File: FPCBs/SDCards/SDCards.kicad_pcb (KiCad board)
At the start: 2 copper layers, 14.7 x 20.5 mm, 4 parts, among them J1 SD_Card_Device, J2 SD_Card_Device, J3 SD_Card_Device, J4 SD_Card_Device

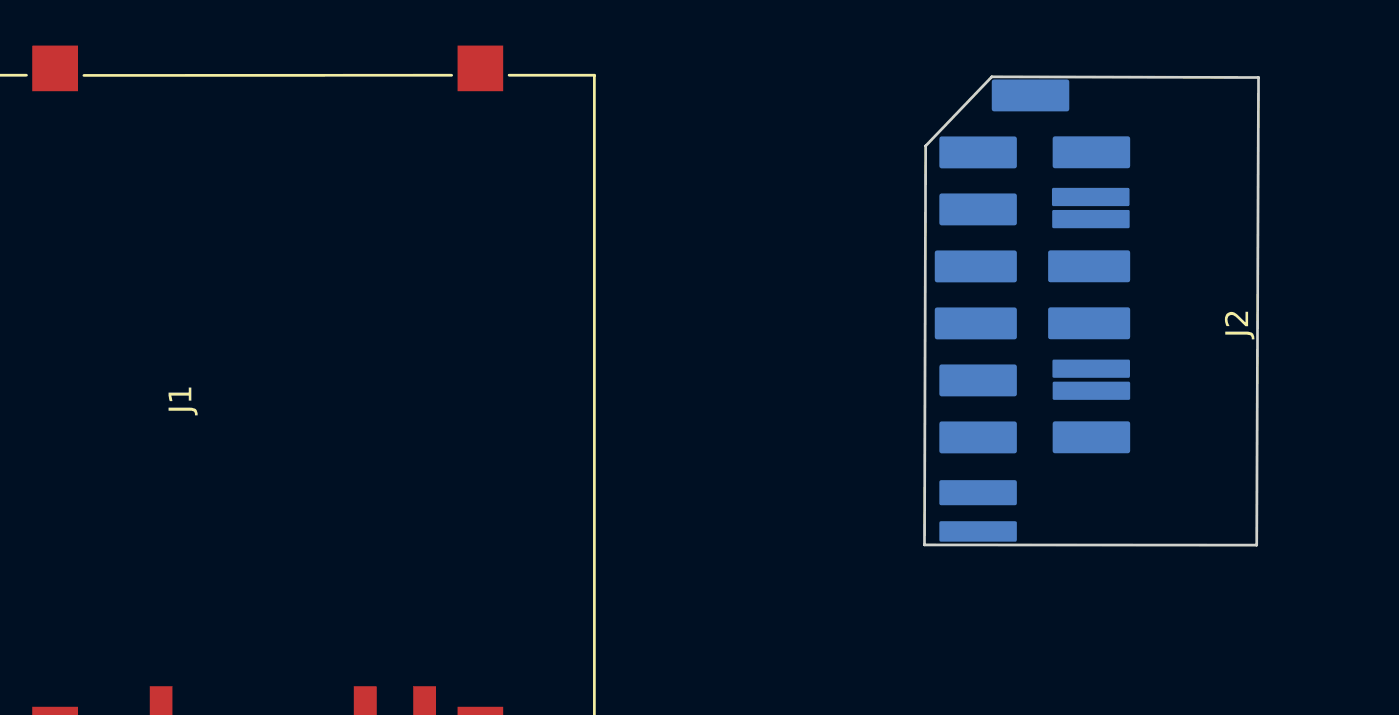
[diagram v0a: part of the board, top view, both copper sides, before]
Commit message: Add pad mask
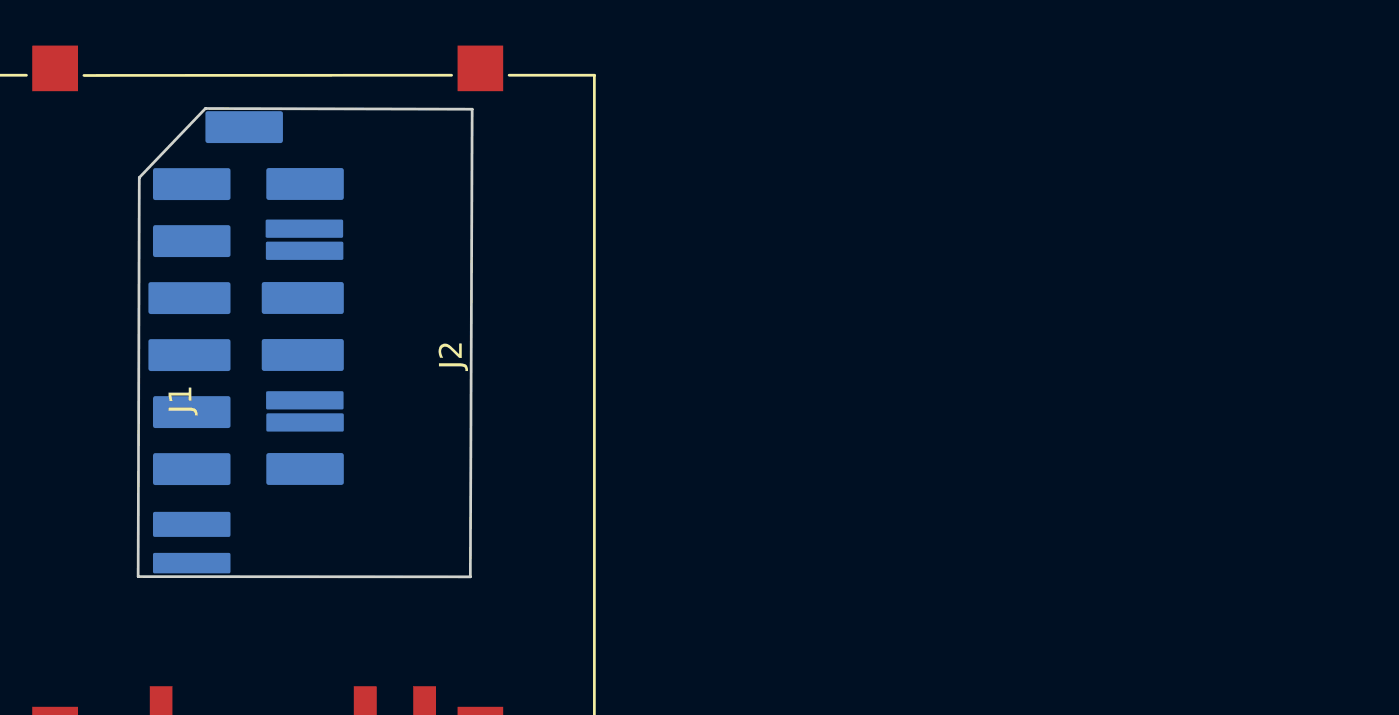
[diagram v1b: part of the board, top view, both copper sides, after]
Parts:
- moved J2 34.5 mm to (82.6, 77.7)
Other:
- outline, holes or cut-outs redrawn
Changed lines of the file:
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@@
 	(footprint "Leica-G9ii:SD_Card_Chip_UHS-II"
 		(layer "F.Cu")
-		(at 117.09 76.325 90)
+		(at 82.6 77.715 90)
 		(descr "SD card device PCB layout, contacts and mechanicalm, 16mm slot depth. Manufacture with PCB thickness of 1.4mm, http://www.convict.lu/pdf/ProdManualSDCardv1.9.pdf")
 		(tags "SD Card")

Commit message: sd card
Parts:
- moved J4 49.9 mm to (89.0, 147.7)
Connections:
- J1 pad 11: (no net) -> Net-(J1-D0+)
- J1 pad 12: (no net) -> Net-(J1-D0-)
- J1 pad 13: (no net) -> Net-(J1-VSS4)
- J1 pad 14: (no net) -> Net-(J1-VDD2)
- J1 pad 15: (no net) -> Net-(J1-D1-)
- J1 pad 16: (no net) -> Net-(J1-D1+)
- J1 pad 17: (no net) -> Net-(J1-Name)
- J1 pad 3: Net-(J1-VSS-Pad3) -> Net-(J1-VSS1)
- J1 pad 6: Net-(J1-VSS-Pad3) -> Net-(J1-VSS2)
- J2 pad 10: (no net) -> Net-(J1-VSS3)
- J2 pad 11: (no net) -> Net-(J1-D0+)
- J2 pad 12: (no net) -> Net-(J1-D0-)
- J2 pad 13: (no net) -> Net-(J1-VSS4)
- J2 pad 14: (no net) -> Net-(J1-VDD2)
- J2 pad 15: (no net) -> Net-(J1-D1-)
- J2 pad 16: (no net) -> Net-(J1-D1+)
- J2 pad 17: (no net) -> Net-(J1-Name)
- J2 pad 3: Net-(J1-VSS-Pad3) -> Net-(J1-VSS1)
- J2 pad 6: Net-(J1-VSS-Pad3) -> Net-(J1-VSS2)
- J3 pad 11: (no net) -> Net-(J3-D0+)
- J3 pad 12: (no net) -> Net-(J3-D0-)
- J3 pad 13: (no net) -> Net-(J3-VSS4)
- J3 pad 14: (no net) -> Net-(J3-VDD2)
- J3 pad 15: (no net) -> Net-(J3-D1-)
- J3 pad 16: (no net) -> Net-(J3-D1+)
- J3 pad 17: (no net) -> Net-(J3-Name)
- J3 pad 3: Net-(J3-VSS-Pad3) -> Net-(J3-VSS1)
- J3 pad 6: Net-(J3-VSS-Pad3) -> Net-(J3-VSS2)
- J4 pad 11: (no net) -> Net-(J3-D0+)
- J4 pad 12: (no net) -> Net-(J3-D0-)
- J4 pad 13: (no net) -> Net-(J3-VSS4)
- J4 pad 14: (no net) -> Net-(J3-VDD2)
- J4 pad 15: (no net) -> Net-(J3-D1-)
- J4 pad 16: (no net) -> Net-(J3-D1+)
- J4 pad 17: (no net) -> Net-(J3-Name)
- J4 pad 3: Net-(J3-VSS-Pad3) -> Net-(J3-VSS1)
- J4 pad 6: Net-(J3-VSS-Pad3) -> Net-(J3-VSS2)
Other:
- board size 14.7 x 20.5 mm -> 45 x 77.4 mm
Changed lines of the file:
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@@
 	(net 2 "Net-(J1-CD{slash}DAT3)")
 	(net 3 "Net-(J1-DAT0)")
-	(net 4 "Net-(J1-VSS-Pad3)")
+	(net 4 "Net-(J1-VDD2)")
 	(net 5 "Net-(J1-CMD)")
 	(net 6 "Net-(J1-DAT1)")
@@
 	(net 8 "Net-(J1-CLK)")
 	(net 9 "Net-(J3-DAT2)")
-	(net 10 "Net-(J3-VSS-Pad3)")
+	(net 10 "Net-(J1-D0-)")
 	(net 11 "Net-(J3-DAT1)")
 	(net 12 "Net-(J3-CLK)")
@@
 	(net 15 "Net-(J3-DAT0)")
 	(net 16 "Net-(J3-CMD)")
+	(net 17 "Net-(J1-VSS4)")
+	(net 18 "Net-(J1-Name)")
+	(net 19 "Net-(J1-VSS1)")
+	(net 20 "Net-(J1-VSS2)")
+	(net 21 "Net-(J1-D0+)")
+	(net 22 "Net-(J1-D1+)")
+	(net 23 "Net-(J1-D1-)")
+	(net 24 "Net-(J1-VSS3)")
+	(net 25 "Net-(J3-VSS2)")
+	(net 26 "Net-(J3-VSS4)")
+	(net 27 "Net-(J3-Name)")
+	(net 28 "Net-(J3-VSS1)")
+	(net 29 "Net-(J3-D0+)")
+	(net 30 "Net-(J3-D1-)")
+	(net 31 "Net-(J3-D0-)")
+	(net 32 "Net-(J3-VDD2)")
+	(net 33 "Net-(J3-D1+)")
 	(footprint "Leica-G9ii:SD_Card_Socket_UHS-II_HTK_AXA573062"
 		(layer "F.Cu")
-		(at 126.44 114.65)
+		(at 89.03 147.69)
 		(descr "SD, SMD, top-mount, push-push (https://www.hirose.com/product/document?clcode=CL0609-0004-8-82&productname=DM1AA-SF-PEJ(82)&series=DM1&documenttype=2DDrawing&lang=en&documentid=0000915301)")
 		(tags "SD card connector")
@@
 			)
 		)
-		(property "Description" "SD card device/card"
+		(property "Description" "SD card UHS-II"
 			(at 0 0 0)
 			(unlocked yes)
@@
 			)
 		)
-		(property ki_fp_filters "SD*Device*")
+		(property ki_fp_filters "SD*")
 		(sheetname "/")
 		(sheetfile "SDCards.kicad_sch")
@@
 			(size 1 2)
 			(layers "F.Cu" "F.Mask" "F.Paste")
-			(net 10 "Net-(J3-VSS-Pad3)")
-			(pinfunction "VSS")
+			(net 28 "Net-(J3-VSS1)")
+			(pinfunction "VSS1")
 			(pintype "power_in")
 		)
@@
 			(size 1 2)
 			(layers "F.Cu" "F.Mask" "F.Paste")
-			(net 10 "Net-(J3-VSS-Pad3)")
-			(pinfunction "VSS")
-			(pintype "passive")
+			(net 25 "Net-(J3-VSS2)")
+			(pinfunction "VSS2")
+			(pintype "power_in")
 		)
 		(pad "7" smd rect
@@
 			(size 1 2)
 			(layers "F.Cu" "F.Mask" "F.Paste")
+			(net 29 "Net-(J3-D0+)")
+			(pinfunction "D0+")
+			(pintype "bidirectional")
 		)
 		(pad "12" smd rect
@@
 			(size 1 2)
 			(layers "F.Cu" "F.Mask" "F.Paste")
+			(net 31 "Net-(J3-D0-)")
+			(pinfunction "D0-")
+			(pintype "bidirectional")
 		)
 		(pad "13" smd rect
@@
 			(size 1 2)
 			(layers "F.Cu" "F.Mask" "F.Paste")
+			(net 26 "Net-(J3-VSS4)")
+			(pinfunction "VSS4")
+			(pintype "power_in")
 		)
 		(pad "14" smd rect
@@
 			(size 1 2)
 			(layers "F.Cu" "F.Mask" "F.Paste")
+			(net 32 "Net-(J3-VDD2)")
+			(pinfunction "VDD2")
+			(pintype "power_in")
 		)
 		(pad "15" smd rect
@@
 			(size 1 2)
 			(layers "F.Cu" "F.Mask" "F.Paste")
+			(net 30 "Net-(J3-D1-)")
+			(pinfunction "D1-")
+			(pintype "bidirectional")
 		)
 		(pad "16" smd rect
@@
 			(size 1 2)
 			(layers "F.Cu" "F.Mask" "F.Paste")
+			(net 33 "Net-(J3-D1+)")
+			(pinfunction "D1+")
+			(pintype "bidirectional")
 		)
 		(pad "17" smd rect
@@
 			(size 1 2)
 			(layers "F.Cu" "F.Mask" "F.Paste")
+			(net 27 "Net-(J3-Name)")
+			(pinfunction "Name")
+			(pintype "power_in")
 		)
 		(pad "CP" smd rect
@@
 			)
 		)
-		(property "Description" "SD card device/card"
+		(property "Description" "SD card UHS-II"
 			(at 0 0 90)
 			(unlocked yes)
@@
 			)
 		)
-		(property ki_fp_filters "SD*Device*")
+		(property ki_fp_filters "SD*")
 		(sheetname "/")
 		(sheetfile "SDCards.kicad_sch")
@@
 			(size 1 2)
 			(layers "F.Cu" "F.Mask" "F.Paste")
-			(net 10 "Net-(J3-VSS-Pad3)")
-			(pinfunction "VSS")
+			(net 28 "Net-(J3-VSS1)")
+			(pinfunction "VSS1")
 			(pintype "power_in")
 		)
@@
 			(size 1 2)
 			(layers "F.Cu" "F.Mask" "F.Paste")
-			(net 10 "Net-(J3-VSS-Pad3)")
-			(pinfunction "VSS")
-			(pintype "passive")
+			(net 25 "Net-(J3-VSS2)")
+			(pinfunction "VSS2")
+			(pintype "power_in")
 		)
 		(pad "7" smd rect
@@
 			(size 1 2)
 			(layers "F.Cu" "F.Mask" "F.Paste")
+			(net 29 "Net-(J3-D0+)")
+			(pinfunction "D0+")
+			(pintype "bidirectional")
 		)
 		(pad "12" smd rect
@@
 			(size 1 2)
 			(layers "F.Cu" "F.Mask" "F.Paste")
+			(net 31 "Net-(J3-D0-)")
+			(pinfunction "D0-")
+			(pintype "bidirectional")
 		)
 		(pad "13" smd rect
@@
 			(size 1 2)
 			(layers "F.Cu" "F.Mask" "F.Paste")
+			(net 26 "Net-(J3-VSS4)")
+			(pinfunction "VSS4")
+			(pintype "power_in")
 		)
 		(pad "14" smd rect
@@
 			(size 1 2)
 			(layers "F.Cu" "F.Mask" "F.Paste")
+			(net 32 "Net-(J3-VDD2)")
+			(pinfunction "VDD2")
+			(pintype "power_in")
 		)
 		(pad "15" smd rect
@@
 			(size 1 2)
 			(layers "F.Cu" "F.Mask" "F.Paste")
+			(net 30 "Net-(J3-D1-)")
+			(pinfunction "D1-")
+			(pintype "bidirectional")
 		)
 		(pad "16" smd rect
@@
 			(size 1 2)
 			(layers "F.Cu" "F.Mask" "F.Paste")
+			(net 33 "Net-(J3-D1+)")
+			(pinfunction "D1+")
+			(pintype "bidirectional")
 		)
 		(pad "17" smd rect
@@
 			(size 1 2)
 			(layers "F.Cu" "F.Mask" "F.Paste")
+			(net 27 "Net-(J3-Name)")
+			(pinfunction "Name")
+			(pintype "power_in")
 		)
 		(pad "CP" smd rect
@@
 			)
 		)
-		(property "Description" "SD card device/card"
+		(property "Description" "SD card UHS-II"
 			(at 0 17.55 90)
 			(unlocked yes)
@@
 			)
 		)
-		(property ki_fp_filters "SD*Device*")
+		(property ki_fp_filters "SD*")
 		(sheetname "/")
 		(sheetfile "SDCards.kicad_sch")
@@
 			(layers "B.Cu" "B.Mask")
 			(roundrect_rratio 0.07142857143)
-			(net 4 "Net-(J1-VSS-Pad3)")
-			(pinfunction "VSS")
+			(net 19 "Net-(J1-VSS1)")
+			(pinfunction "VSS1")
 			(pintype "power_in")
 			(clearance 0.05)
@@
 			(layers "B.Cu" "B.Mask")
 			(roundrect_rratio 0.07142857143)
-			(net 4 "Net-(J1-VSS-Pad3)")
-			(pinfunction "VSS")
-			(pintype "passive")
+			(net 20 "Net-(J1-VSS2)")
+			(pinfunction "VSS2")
+			(pintype "power_in")
 			(clearance 0.05)
 		)
@@
 			(layers "B.Cu" "B.Mask")
 			(roundrect_rratio 0.07142857143)
+			(net 24 "Net-(J1-VSS3)")
+			(pinfunction "VSS3")
+			(pintype "power_in")
 			(clearance 0.05)
 		)
@@
 			(layers "B.Cu" "B.Mask")
 			(roundrect_rratio 0.07142857143)
+			(net 21 "Net-(J1-D0+)")
+			(pinfunction "D0+")
+			(pintype "bidirectional")
 			(clearance 0.05)
 		)
@@
 			(layers "B.Cu" "B.Mask")
 			(roundrect_rratio 0.07142857143)
+			(net 10 "Net-(J1-D0-)")
+			(pinfunction "D0-")
+			(pintype "bidirectional")
 			(clearance 0.05)
 		)
@@
 			(layers "B.Cu" "B.Mask")
 			(roundrect_rratio 0.07142857143)
+			(net 17 "Net-(J1-VSS4)")
+			(pinfunction "VSS4")
+			(pintype "power_in")
 			(clearance 0.05)
 		)
@@
 			(layers "B.Cu" "B.Mask")
 			(roundrect_rratio 0.07142857143)
+			(net 4 "Net-(J1-VDD2)")
+			(pinfunction "VDD2")
+			(pintype "power_in")
 			(clearance 0.05)
 		)
@@
 			(layers "B.Cu" "B.Mask")
 			(roundrect_rratio 0.07142857143)
+			(net 23 "Net-(J1-D1-)")
+			(pinfunction "D1-")
+			(pintype "bidirectional")
 			(clearance 0.05)
 		)
@@
 			(layers "B.Cu" "B.Mask")
 			(roundrect_rratio 0.07142857143)
+			(net 22 "Net-(J1-D1+)")
+			(pinfunction "D1+")
+			(pintype "bidirectional")
 			(clearance 0.05)
 		)
@@
 			(layers "B.Cu" "B.Mask")
 			(roundrect_rratio 0.07142857143)
+			(net 18 "Net-(J1-Name)")
+			(pinfunction "Name")
+			(pintype "power_in")
 			(clearance 0.05)
 		)
@@
 			)
 		)
-		(property "Description" "SD card device/card"
+		(property "Description" "SD card UHS-II"
 			(at 0 0 90)
 			(unlocked yes)
@@
 			)
 		)
-		(property ki_fp_filters "SD*Device*")
+		(property ki_fp_filters "SD*")
 		(sheetname "/")
 		(sheetfile "SDCards.kicad_sch")
@@
 			(size 1 2)
 			(layers "F.Cu" "F.Mask" "F.Paste")
-			(net 4 "Net-(J1-VSS-Pad3)")
-			(pinfunction "VSS")
+			(net 19 "Net-(J1-VSS1)")
+			(pinfunction "VSS1")
 			(pintype "power_in")
 		)
@@
 			(size 1 2)
 			(layers "F.Cu" "F.Mask" "F.Paste")
-			(net 4 "Net-(J1-VSS-Pad3)")
-			(pinfunction "VSS")
-			(pintype "passive")
+			(net 20 "Net-(J1-VSS2)")
+			(pinfunction "VSS2")
+			(pintype "power_in")
 		)
 		(pad "7" smd rect
@@
 			(size 1 2)
 			(layers "F.Cu" "F.Mask" "F.Paste")
+			(net 21 "Net-(J1-D0+)")
+			(pinfunction "D0+")
+			(pintype "bidirectional")
 		)
 		(pad "12" smd rect
@@
 			(size 1 2)
 			(layers "F.Cu" "F.Mask" "F.Paste")
+			(net 10 "Net-(J1-D0-)")
+			(pinfunction "D0-")
+			(pintype "bidirectional")
 		)
 		(pad "13" smd rect
@@
 			(size 1 2)
 			(layers "F.Cu" "F.Mask" "F.Paste")
+			(net 17 "Net-(J1-VSS4)")
+			(pinfunction "VSS4")
+			(pintype "power_in")
 		)
 		(pad "14" smd rect
@@
 			(size 1 2)
 			(layers "F.Cu" "F.Mask" "F.Paste")
+			(net 4 "Net-(J1-VDD2)")
+			(pinfunction "VDD2")
+			(pintype "power_in")
 		)
 		(pad "15" smd rect
@@
 			(size 1 2)
 			(layers "F.Cu" "F.Mask" "F.Paste")
+			(net 23 "Net-(J1-D1-)")
+			(pinfunction "D1-")
+			(pintype "bidirectional")
 		)
 		(pad "16" smd rect
@@
 			(size 1 2)
 			(layers "F.Cu" "F.Mask" "F.Paste")
+			(net 22 "Net-(J1-D1+)")
+			(pinfunction "D1+")
+			(pintype "bidirectional")
 		)
 		(pad "17" smd rect
@@
 			(size 1 2)
 			(layers "F.Cu" "F.Mask" "F.Paste")
+			(net 18 "Net-(J1-Name)")
+			(pinfunction "Name")
+			(pintype "power_in")
 		)
 		(pad "CP" smd rect
@@
 		)
 	)
+	(gr_line
+		(start 68.11 139.02)
+		(end 113.14 139.15)
+		(stroke
+			(width 0.05)
+			(type default)
+		)
+		(layer "Edge.Cuts")
+	)
+	(gr_line
+		(start 68.11 61.76)
+		(end 68.11 139.02)
+		(stroke
+			(width 0.05)
+			(type default)
+		)
+		(layer "Edge.Cuts")
+	)
+	(gr_line
+		(start 68.11 61.76)
+		(end 113.14 61.76)
+		(stroke
+			(width 0.05)
+			(type default)
+		)
+		(layer "Edge.Cuts")
+	)
+	(gr_line
+		(start 113.14 61.76)
+		(end 113.14 139.15)
+		(stroke
+			(width 0.05)
+			(type default)
+		)
+		(layer "Edge.Cuts")
+	)
 	(embedded_fonts no)

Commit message: Fix sd card
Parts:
- J1, J3: footprint Leica-G9ii:SD_Card_Socket_UHS-II_HTK_AXA573062 -> Leica-G9ii:SD_Card_Socket_UHS-II_Extender
- J4: moved to B.Cu
- moved J4 54.3 mm to (125.2, 107.2), turned to 180 degrees
- moved J3 5.57 mm to (86.8, 109.2)
- moved J2 2.56 mm to (80.7, 79.4)
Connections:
- J1 pad WP: (no net) -> Net-(J1-CARD_DETECT)
- J2 pad 10: Net-(J1-VSS3) -> Net-(J1-VSS1)
- J3 pad WP: (no net) -> Net-(J3-WRITE_PROTECT)
- J4 pad WP: (no net) -> Net-(J3-WRITE_PROTECT)
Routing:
- net Net-(J3-DAT1): track 0.00 -> 77.3 mm
- net Net-(J3-DAT0): track 0.00 -> 75.0 mm
- net Net-(J3-VSS2): track 0.00 -> 71.7 mm
- net Net-(J3-D1-): track 0.00 -> 69.8 mm
- net Net-(J3-D1+): track 0.00 -> 68.0 mm
- net Net-(J3-CLK): track 0.00 -> 66.4 mm
- net Net-(J3-CARD_DETECT): track 0.00 -> 65.0 mm
- net Net-(J3-Name): track 0.00 -> 64.6 mm
- net Net-(J3-VDD): track 0.00 -> 62.8 mm
- net Net-(J3-VDD2): track 0.00 -> 61.1 mm
- net Net-(J3-VSS1): track 0.00 -> 59.3 mm
- net Net-(J3-CMD): track 0.00 -> 57.6 mm
- net Net-(J3-D0+): track 0.00 -> 55.8 mm
- net Net-(J3-D0-): track 0.00 -> 54.0 mm
- net Net-(J3-WRITE_PROTECT): track 0.00 -> 52.6 mm
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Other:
- board size 45 x 77.4 mm -> 73.7 x 61.1 mm

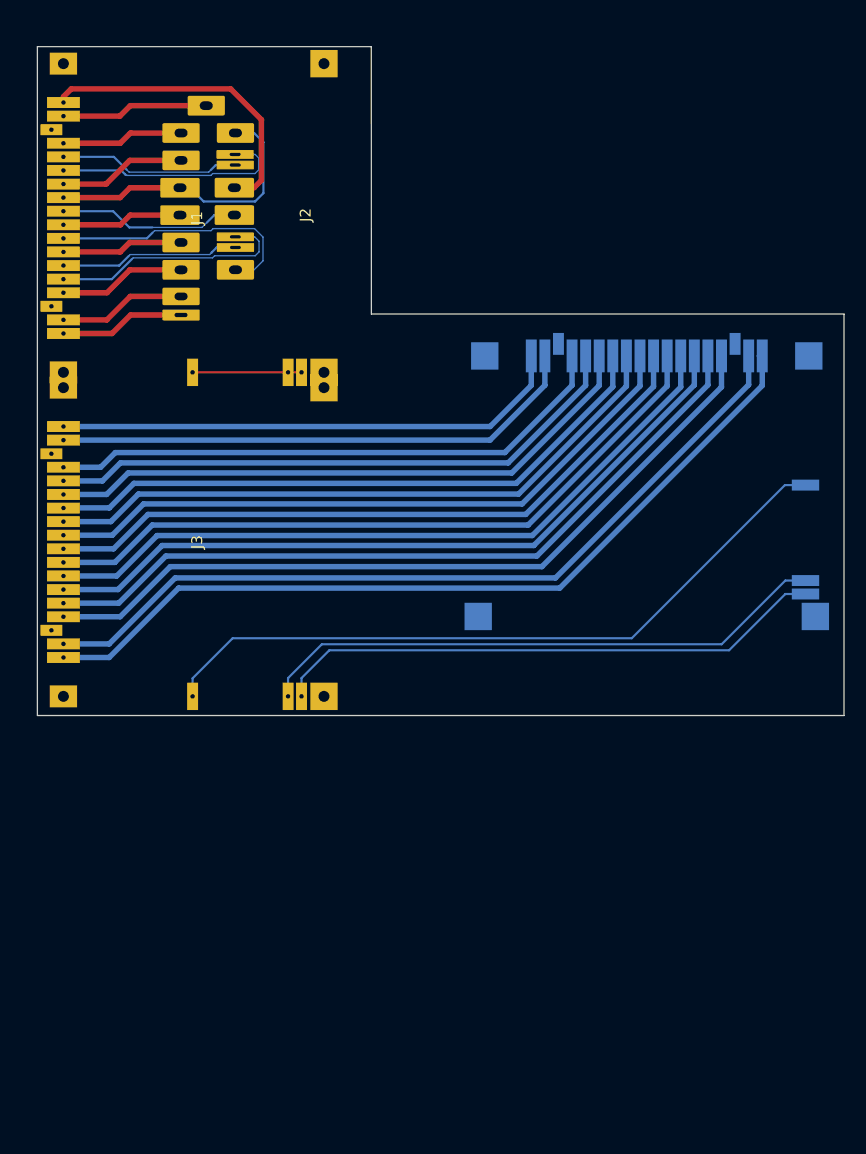
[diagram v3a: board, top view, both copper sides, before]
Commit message: Fix spacings and pads
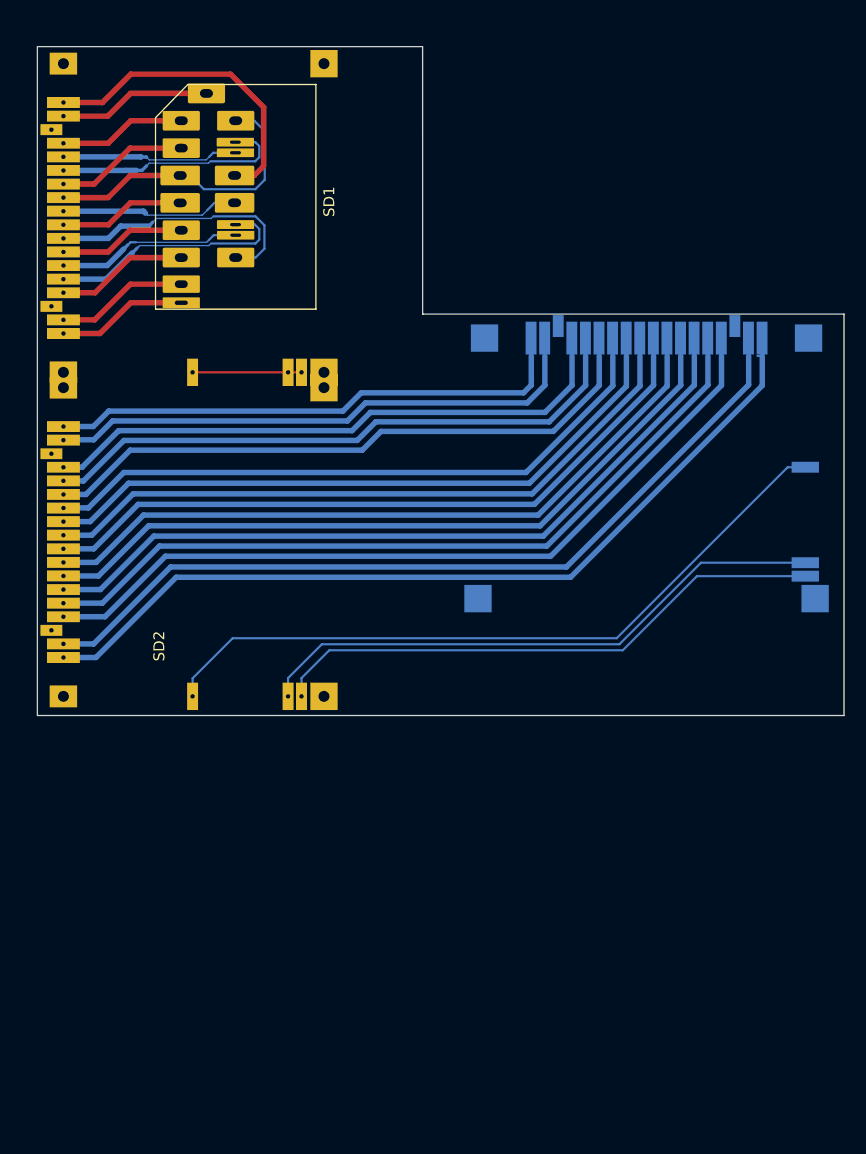
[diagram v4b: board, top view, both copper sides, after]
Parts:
- J1, J2: value SD_Card_Device -> SD1
- J3, J4: value SD_Card_Device -> SD2
- moved J4 1.63 mm to (125.2, 105.5)
- moved J2 1.12 mm to (80.7, 78.3)
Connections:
- J1 pad SH: (no net) -> Net-(J1-SHIELD)
- J3 pad SH: (no net) -> Net-(J1-SHIELD)
- J4 pad SH: (no net) -> Net-(J1-SHIELD)
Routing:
- net Net-(J1-D1+): track 16.4 -> 17.4 mm
- net Net-(J1-Name): track 23.9 -> 24.6 mm
- net Net-(J1-D0-): track 16.5 -> 15.9 mm
- net Net-(J3-COMMON): track 50.9 -> 51.5 mm
- net Net-(J3-WRITE_PROTECT): track 52.6 -> 53.3 mm
- net Net-(J3-CARD_DETECT): track 65.0 -> 65.6 mm
- net Net-(J1-VSS4): track 28.4 -> 29.0 mm
- net Net-(J1-VSS1): track 27.0 -> 27.6 mm
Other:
- outline, holes or cut-outs redrawn
